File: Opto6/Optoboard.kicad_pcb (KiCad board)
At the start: 2 copper layers, 91.4 x 33 mm, 54 parts, among them J1 S1 Connector, J2 S2 Connector, J3 S3 Connector, J4 S4 Connector, J6 S5 Connector, J7 S6 Connector, P1 CONN_01X08, Q1 IRLR024NPBF, U1 6N135, U2 6N135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

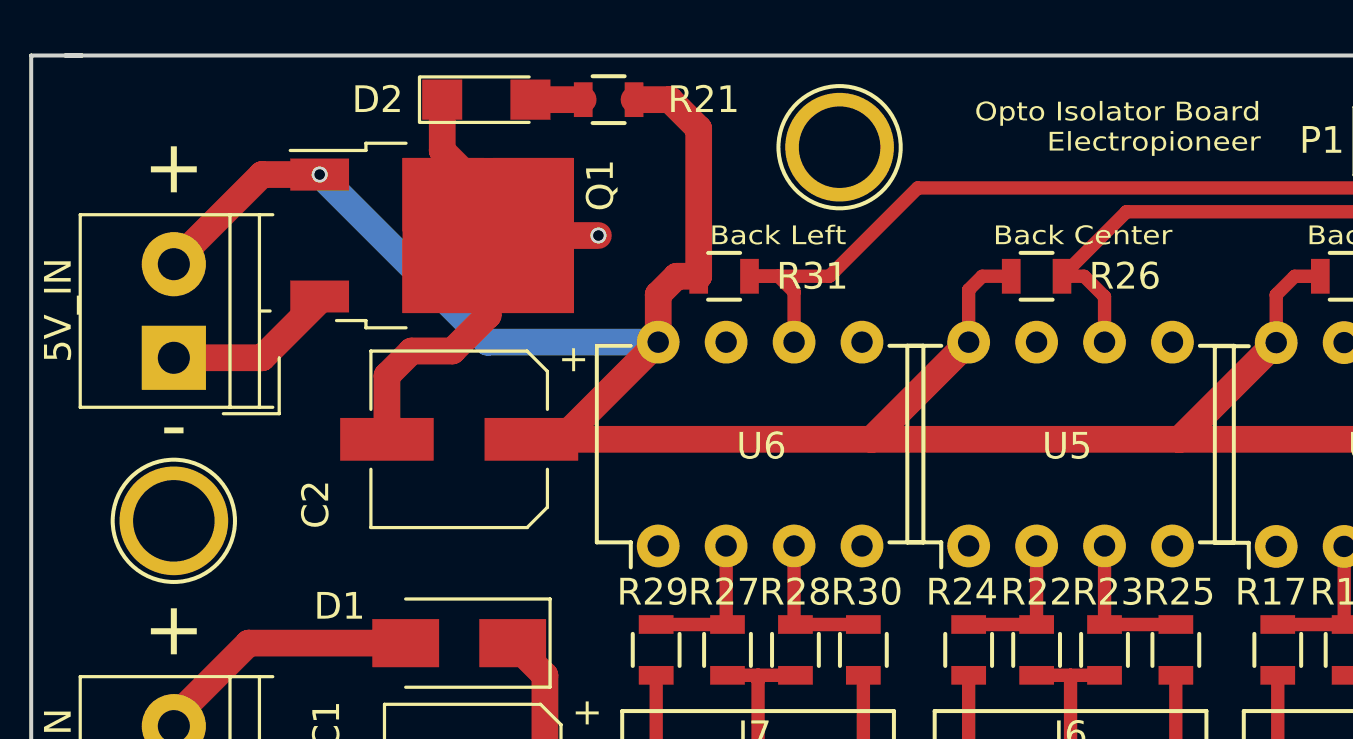
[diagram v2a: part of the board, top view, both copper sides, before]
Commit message: Cleaned up, no more bottom trace, only plain
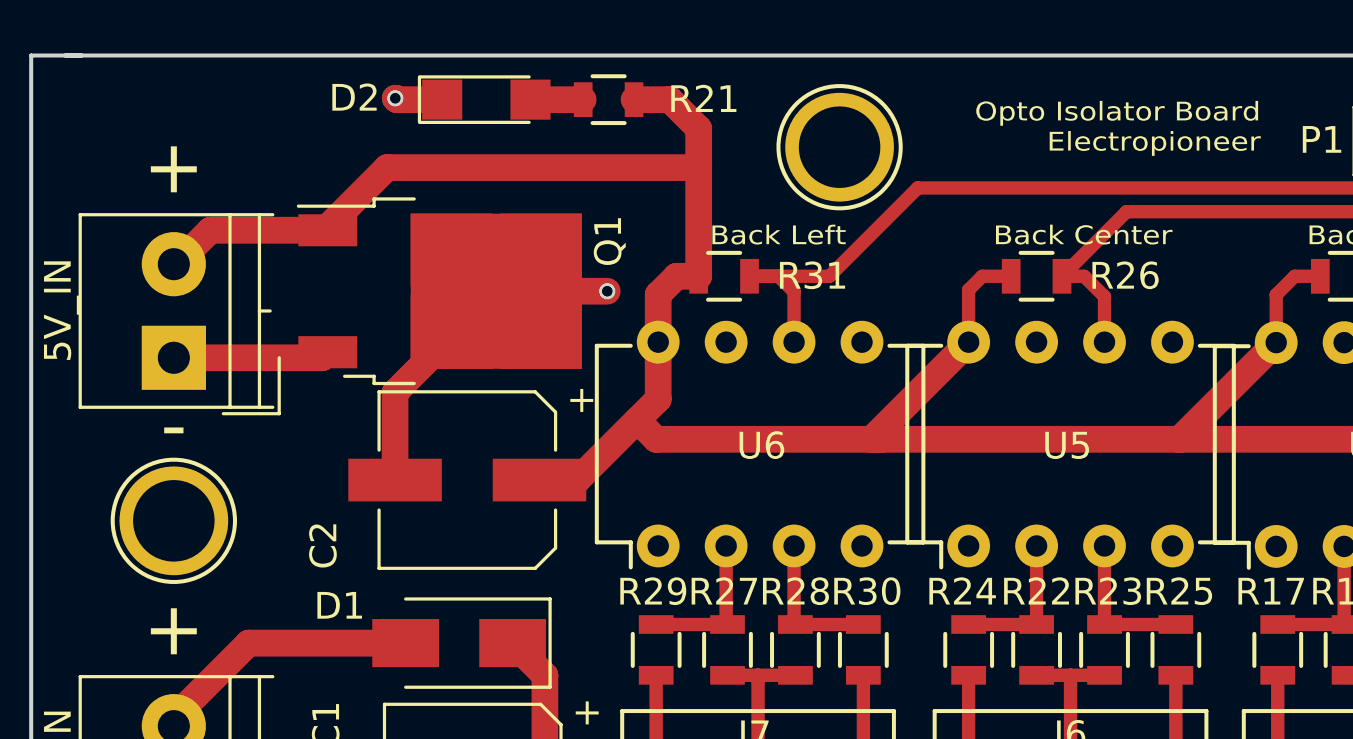
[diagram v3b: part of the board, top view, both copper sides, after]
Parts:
- moved Q1 2.10 mm to (151.7, 99.0)
- moved C2 1.55 mm to (152.8, 106.0)
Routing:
- net GND: track 61.2 -> 55.8 mm, vias 1 -> 2
- net +5V: track 190.2 -> 187.6 mm, vias 1 -> 0
- net Net-(5V_IN1-Pad1): track 6.48 -> 5.84 mm
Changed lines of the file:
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@@
     (links 107)
     (no_connects 0)
-    (area 120.734087 84.3736 238.4288 125.673172)
+    (area 136.373799 90.069599 227.963801 123.239601)
     (thickness 1.6)
     (drawings 49)
-    (tracks 229)
+    (tracks 232)
     (zones 0)
     (modules 54)
@@
   )
   (module TO_SOT_Packages_SMD:TO-252-2 (layer F.Cu)
-    (at 151.4348 96.8756)
+    (at 151.7396 98.9584)
     (descr "TO-252 / DPAK SMD package, http://www.infineon.com/cms/en/product/packages/PG-TO252/PG-TO252-3-1/")
     (tags "DPAK TO-252 DPAK-3 TO-252-3 SOT-428")
@@
   )
   (module Capacitors_SMD:CP_Elec_6.3x5.3 (layer F.Cu)
-    (at 152.4508 104.4956 180)
+    (at 152.7556 106.0196 180)
     (descr "SMT capacitor, aluminium electrolytic, 6.3x5.3")
     (attr smd)
@@
     (effects (font (size 0.7 0.8) (thickness 0.175)) (justify right))
   )
-  (gr_text "D2\n" (at 149.4028 91.7956) (layer F.SilkS)
+  (gr_text "D2\n" (at 148.5392 91.7448) (layer F.SilkS)
     (effects (font (size 1 1) (thickness 0.15)))
   )
@@
     (effects (font (size 2 2) (thickness 0.3)))
   )
-  (segment (start 153.5348 96.8756) (end 157.6578 96.8756) (width 1) (layer F.Cu) (net 1))
-  (via (at 157.6578 96.8756) (size 0.6) (drill 0.4) (layers F.Cu B.Cu) (net 1))
+  (segment (start 153.8396 98.9584) (end 157.988 98.9584) (width 1) (layer F.Cu) (net 1) (status 400000))
+  (via (at 157.988 98.9584) (size 0.6) (drill 0.4) (layers F.Cu B.Cu) (net 1))
+  (segment (start 151.8168 91.7956) (end 150.114 91.7956) (width 1) (layer F.Cu) (net 1) (status 400000))
+  (segment (start 150.0632 91.7448) (end 150.114 91.7448) (width 1) (layer B.Cu) (net 1))
+  (via (at 150.0632 91.7448) (size 0.6) (drill 0.4) (layers F.Cu B.Cu) (net 1))
+  (segment (start 150.114 91.7956) (end 150.0632 91.7448) (width 1) (layer F.Cu) (net 1))
+  (segment (start 150.0556 106.0196) (end 150.0556 102.7424) (width 1) (layer F.Cu) (net 1) (status 400000))
+  (segment (start 150.0556 102.7424) (end 153.8396 98.9584) (width 1) (layer F.Cu) (net 1) (status 800000))
   (segment (start 167.513 100.5078) (end 167.513 100.8634) (width 0.5) (layer B.Cu) (net 1))
   (segment (start 141.7828 118.7196) (end 149.2428 118.7196) (width 1) (layer F.Cu) (net 1))
@@
   (segment (start 167.5638 113.3196) (end 167.5638 116.6876) (width 0.5) (layer F.Cu) (net 1))
   (segment (start 167.5638 116.6876) (end 166.1668 118.0846) (width 0.5) (layer F.Cu) (net 1))
-  (segment (start 153.5348 96.8756) (end 153.5348 95.4196) (width 1) (layer F.Cu) (net 1))
-  (segment (start 153.5348 95.4196) (end 151.8168 93.7016) (width 1) (layer F.Cu) (net 1))
-  (segment (start 151.8168 93.7016) (end 151.8168 91.7956) (width 1) (layer F.Cu) (net 1))
-  (segment (start 153.5348 96.8756) (end 153.5348 99.8556) (width 1) (layer F.Cu) (net 1))
-  (segment (start 153.5348 99.8556) (end 152.1968 101.1936) (width 1) (layer F.Cu) (net 1))
-  (segment (start 152.1968 101.1936) (end 150.6728 101.1936) (width 1) (layer F.Cu) (net 1))
-  (segment (start 150.6728 101.1936) (end 149.7508 102.1156) (width 1) (layer F.Cu) (net 1))
-  (segment (start 149.7508 102.1156) (end 149.7508 104.4956) (width 1) (layer F.Cu) (net 1))
   (segment (start 141.7828 115.2196) (end 141.7828 114.9096) (width 1) (layer F.Cu) (net 2))
   (segment (start 141.7828 114.9096) (end 144.5768 112.1156) (width 1) (layer F.Cu) (net 2))
@@
   (segment (start 159.8168 116.7746) (end 161.1268 118.0846) (width 0.5) (layer F.Cu) (net 3))
   (segment (start 184.22 117.895) (end 184.42 118.095) (width 0.5) (layer F.Cu) (net 3))
-  (segment (start 159.893 100.8634) (end 159.893 99.0854) (width 1) (layer F.Cu) (net 4) (status 400000))
+  (segment (start 168.2496 104.4956) (end 159.8168 104.4956) (width 1) (layer F.Cu) (net 4))
+  (segment (start 159.8168 104.4956) (end 159.1056 103.7844) (width 1) (layer F.Cu) (net 4))
+  (segment (start 155.4556 106.0196) (end 156.8704 106.0196) (width 1) (layer F.Cu) (net 4) (status C00000))
+  (segment (start 156.8704 106.0196) (end 159.1056 103.7844) (width 1) (layer F.Cu) (net 4) (status 400000))
+  (segment (start 159.1056 103.7844) (end 159.893 102.997) (width 1) (layer F.Cu) (net 4))
+  (segment (start 159.893 102.997) (end 159.893 100.8634) (width 1) (layer F.Cu) (net 4) (status 800000))
+  (segment (start 147.5396 96.6784) (end 147.5396 96.5544) (width 1) (layer F.Cu) (net 4) (status C00000))
+  (segment (start 147.5396 96.5544) (end 149.7584 94.3356) (width 1) (layer F.Cu) (net 4) (status 400000))
+  (segment (start 149.7584 94.3356) (end 161.4068 94.3356) (width 1) (layer F.Cu) (net 4))
+  (segment (start 141.7828 97.9476) (end 141.8792 97.9476) (width 1) (layer F.Cu) (net 4) (status C00000))
+  (segment (start 141.8792 97.9476) (end 143.1484 96.6784) (width 1) (layer F.Cu) (net 4) (status 400000))
+  (segment (start 143.1484 96.6784) (end 147.5396 96.6784) (width 1) (layer F.Cu) (net 4) (status 800000))
+  (segment (start 159.893 100.8634) (end 159.893 99.0854) (width 1) (layer F.Cu) (net 4))
   (segment (start 159.893 99.0854) (end 160.5788 98.3996) (width 1) (layer F.Cu) (net 4))
-  (segment (start 160.5788 98.3996) (end 161.4068 98.3996) (width 1) (layer F.Cu) (net 4) (status 800000))
+  (segment (start 160.5788 98.3996) (end 161.4068 98.3996) (width 1) (layer F.Cu) (net 4))
   (segment (start 202.3844 104.4956) (end 213.8844 104.4956) (width 1) (layer F.Cu) (net 4))
-  (segment (start 213.8844 104.4956) (end 217.5 100.88) (width 1) (layer F.Cu) (net 4) (status 800000))
+  (segment (start 213.8844 104.4956) (end 217.5 100.88) (width 1) (layer F.Cu) (net 4))
   (segment (start 190.8844 104.4956) (end 202.3844 104.4956) (width 1) (layer F.Cu) (net 4))
-  (segment (start 202.3844 104.4956) (end 206 100.88) (width 1) (layer F.Cu) (net 4) (status 800000))
+  (segment (start 202.3844 104.4956) (end 206 100.88) (width 1) (layer F.Cu) (net 4))
   (segment (start 179.3748 104.4956) (end 190.8844 104.4956) (width 1) (layer F.Cu) (net 4))
-  (segment (start 190.8844 104.4956) (end 194.5 100.88) (width 1) (layer F.Cu) (net 4) (status 800000))
-  (segment (start 167.8686 104.4956) (end 179.3748 104.4956) (width 1) (layer F.Cu) (net 4))
+  (segment (start 190.8844 104.4956) (end 194.5 100.88) (width 1) (layer F.Cu) (net 4))
+  (segment (start 167.8686 104.4956) (end 168.2496 104.4956) (width 1) (layer F.Cu) (net 4))
+  (segment (start 168.2496 104.4956) (end 179.3748 104.4956) (width 1) (layer F.Cu) (net 4))
   (segment (start 179.3748 104.4956) (end 179.3844 104.4956) (width 1) (layer F.Cu) (net 4))
-  (segment (start 179.3844 104.4956) (end 183 100.88) (width 1) (layer F.Cu) (net 4) (status 800000))
-  (segment (start 155.1508 104.4956) (end 167.8686 104.4956) (width 1) (layer F.Cu) (net 4) (status 400000))
-  (segment (start 167.8686 104.4956) (end 171.5008 100.8634) (width 1) (layer F.Cu) (net 4) (status 800000))
-  (via (at 147.2348 94.5956) (size 0.6) (drill 0.4) (layers F.Cu B.Cu) (net 4))
-  (segment (start 145.0788 94.5956) (end 147.2348 94.5956) (width 1) (layer F.Cu) (net 4))
-  (segment (start 141.7828 97.8916) (end 145.0788 94.5956) (width 1) (layer F.Cu) (net 4))
-  (segment (start 153.5026 100.8634) (end 159.893 100.8634) (width 1) (layer B.Cu) (net 4))
-  (segment (start 147.2348 94.5956) (end 153.5026 100.8634) (width 1) (layer B.Cu) (net 4))
+  (segment (start 179.3844 104.4956) (end 183 100.88) (width 1) (layer F.Cu) (net 4))
+  (segment (start 167.8686 104.4956) (end 171.5008 100.8634) (width 1) (layer F.Cu) (net 4))
   (segment (start 141.7828 97.9476) (end 141.7828 97.8916) (width 1) (layer F.Cu) (net 4))
   (segment (start 204.978 93.345) (end 204.978 99.858) (width 0.5) (layer B.Cu) (net 4))
@@
   (segment (start 159.893 99.0854) (end 160.5788 98.3996) (width 0.5) (layer F.Cu) (net 4))
   (segment (start 160.5788 98.3996) (end 161.4068 98.3996) (width 0.5) (layer F.Cu) (net 4))
-  (segment (start 155.1508 104.4956) (end 156.2608 104.4956) (width 1) (layer F.Cu) (net 4))
-  (segment (start 156.2608 104.4956) (end 159.893 100.8634) (width 1) (layer F.Cu) (net 4))
   (segment (start 158.9888 91.7956) (end 160.3248 91.7956) (width 1) (layer F.Cu) (net 4))
-  (segment (start 161.4068 92.8776) (end 161.4068 98.3996) (width 1) (layer F.Cu) (net 4))
+  (segment (start 161.4068 92.8776) (end 161.4068 94.3356) (width 1) (layer F.Cu) (net 4))
+  (segment (start 161.4068 94.3356) (end 161.4068 98.3996) (width 1) (layer F.Cu) (net 4))
   (segment (start 160.3248 91.7956) (end 161.4068 92.8776) (width 1) (layer F.Cu) (net 4))
   (segment (start 141.7828 97.9476) (end 141.7828 97.3836) (width 1) (layer F.Cu) (net 4))
@@
   (segment (start 188.08 108.5) (end 188.08 111.2348) (width 0.5) (layer F.Cu) (net 20))
   (segment (start 188.08 111.2348) (end 188.2648 111.4196) (width 0.5) (layer F.Cu) (net 20))
-  (segment (start 141.7828 101.4476) (end 145.0848 101.4476) (width 1) (layer F.Cu) (net 21))
-  (segment (start 145.0848 101.4476) (end 147.2348 99.2976) (width 1) (layer F.Cu) (net 21))
-  (segment (start 147.2348 99.2976) (end 147.2348 99.1556) (width 1) (layer F.Cu) (net 21))
+  (segment (start 141.7828 101.4476) (end 147.3304 101.4476) (width 1) (layer F.Cu) (net 21) (status C00000))
+  (segment (start 147.3304 101.4476) (end 147.5396 101.2384) (width 1) (layer F.Cu) (net 21) (status C00000))
   (segment (start 174.0408 111.4196) (end 171.5008 111.4196) (width 0.5) (layer F.Cu) (net 22))
   (segment (start 174.0408 108.4834) (end 174.0408 111.4196) (width 0.5) (layer F.Cu) (net 22))

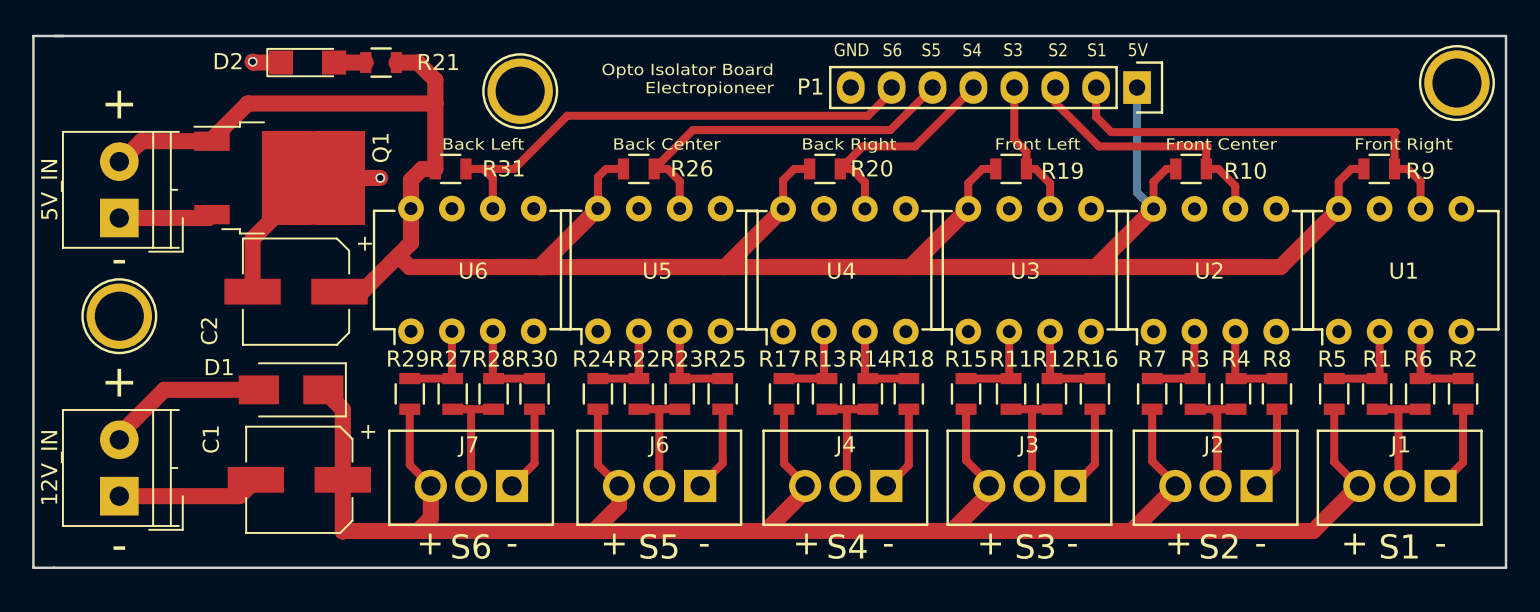
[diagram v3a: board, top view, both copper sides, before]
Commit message: Added output files for both version
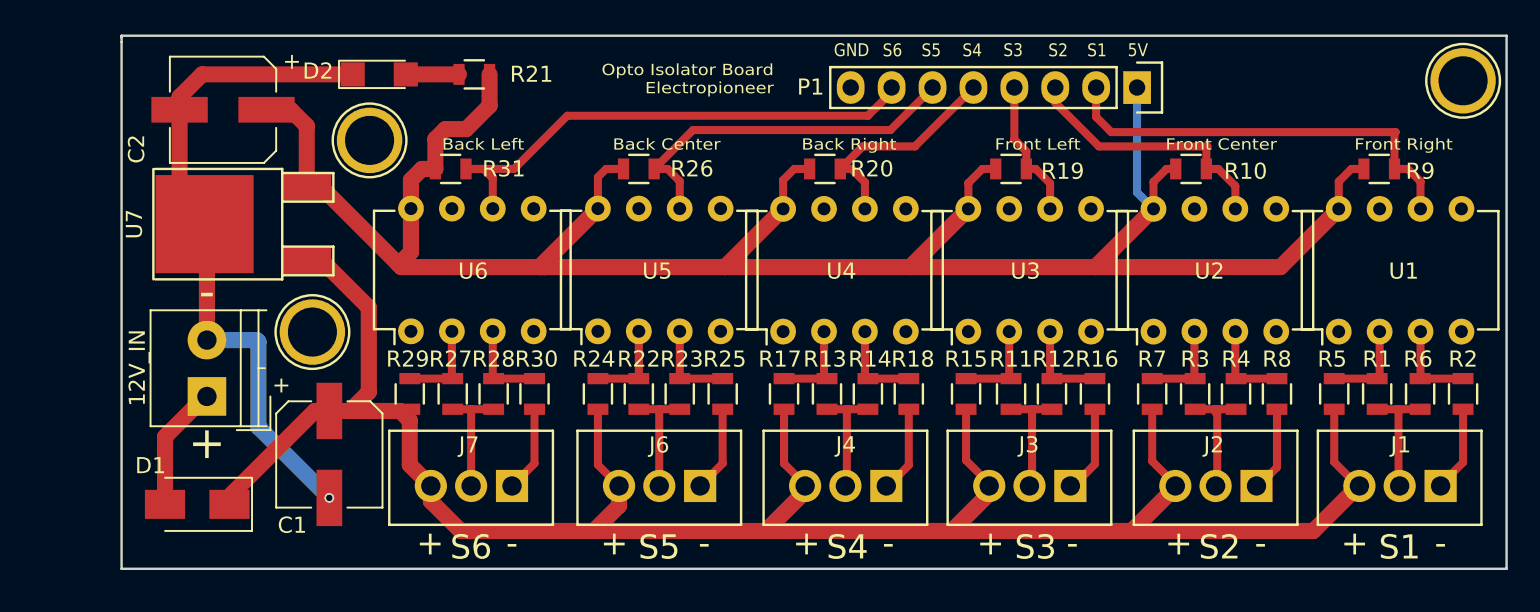
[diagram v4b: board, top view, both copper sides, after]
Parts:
- removed 5V_IN: Screw_Terminal_01x02, Connectors_Terminal_Blocks:TerminalBlock_4UCON_19963_02x3.5mm_Straight
- removed Q1: IRLR024NPBF, TO_SOT_Packages_SMD:TO-252-2
- removed the REF** at (141.8, 107.5)
- removed the REF** at (224.8, 93.1)
- removed the REF** at (166.7, 93.6)
- added REF**: 1pin, Connect:1pin, F.Cu at (157.3, 96.6)
- added REF**: 1pin, Connect:1pin, F.Cu at (225.2, 92.9)
- added REF**: 1pin, Connect:1pin, F.Cu at (153.8, 108.5)
- added U7: L7805, TO_SOT_Packages_SMD:TO-252-2Lead, F.Cu at (153.4, 101.8)
- moved C2 12.2 mm to (148.2, 94.7)
- moved D1 9.19 mm to (146.6, 119.2)
- moved 12V_IN 8.24 mm to (147.2, 112.5)
- moved R21 5.83 mm to (163.8, 92.5)
- moved D2 4.52 mm to (157.9, 92.5)
- moved C1 2.44 mm to (154.8, 116.1), turned to 270 degrees
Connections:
- 12V_IN pad 1: GND -> Net-(12V_IN1-Pad1)
- 12V_IN pad 2: Net-(12V_IN1-Pad2) -> GND
- D1 pad 2: Net-(12V_IN1-Pad2) -> Net-(12V_IN1-Pad1)
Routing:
- net GND: track 55.8 -> 74.2 mm, vias 2 -> 1
- net +12V: track 124.1 -> 136.9 mm
- net +5V: track 187.6 -> 175.6 mm
- net Net-(12V_IN1-Pad2): track 10.1 -> 0.00 mm
- net Net-(12V_IN1-Pad1): track 0.00 -> 7.84 mm
- net Net-(5V_IN1-Pad1): track 5.84 -> 0.00 mm
- net Net-(D2-Pad2): track 1.97 -> 3.30 mm
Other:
- board size 91.4 x 33 mm -> 86 x 33.1 mm

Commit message: Added files
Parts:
- removed the REF** at (157.3, 96.6)
- removed the REF** at (225.2, 92.9)
- removed the REF** at (153.8, 108.5)
- added P2: CONN_01X02, Pin_Headers:Pin_Header_Straight_1x02, F.Cu at (211.8, 93.3)
- added REF**: 1pin, Connect:1pin, F.Cu at (224.5, 93.5)
- added REF**: 1pin, Connect:1pin, F.Cu at (154.3, 108.8)
- added REF**: 1pin, Connect:1pin, F.Cu at (157.6, 96.7)
- moved 12V_IN 2.86 mm to (146.0, 115.1)
- moved C1 1.60 mm to (154.7, 117.7)
- moved D1 1.50 mm to (146.5, 120.7)
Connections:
- P1 pad 1: +5V -> Net-(P1-Pad1)
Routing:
- net Net-(P1-Pad1): track 0.00 -> 6.85 mm
- net +12V: track 136.9 -> 143.6 mm
- net GND: track 74.2 -> 76.6 mm
- net Net-(12V_IN1-Pad1): track 7.84 -> 6.43 mm
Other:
- board text added: "EN 5V"
